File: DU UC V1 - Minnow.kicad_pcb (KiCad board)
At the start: 4 copper layers, 30 x 69.6 mm, 158 parts, among them J1701 MicroUSB, J1801 Conn_01x06_Pin, J1802 Conn_01x04_Pin, J201 SODIMM-260, Q1301 BSS84, Q1501 BSS84, Q1502 BSS84, Q1701 MMBT3904, Q701 BSS84, Q702 BSS84, SW401 STLINK_RST, SW501 MCU_RST, U1101 74HC4051, U1401 TPS25961, U1402 TPS25961, U1501 TCAN334G, U1701 PSM712-LF-T7, U301 TPS7B8733QKVURQ1, U401 STM32F103CBTx, U501 STM32L552ZET6Q, U701 TCAN334G, U901 MX25R3235FM2xx1, Y401 8MHz 5pF, Y501 32.768kHz, 1.2pF, Y502 16MHz, 7pF

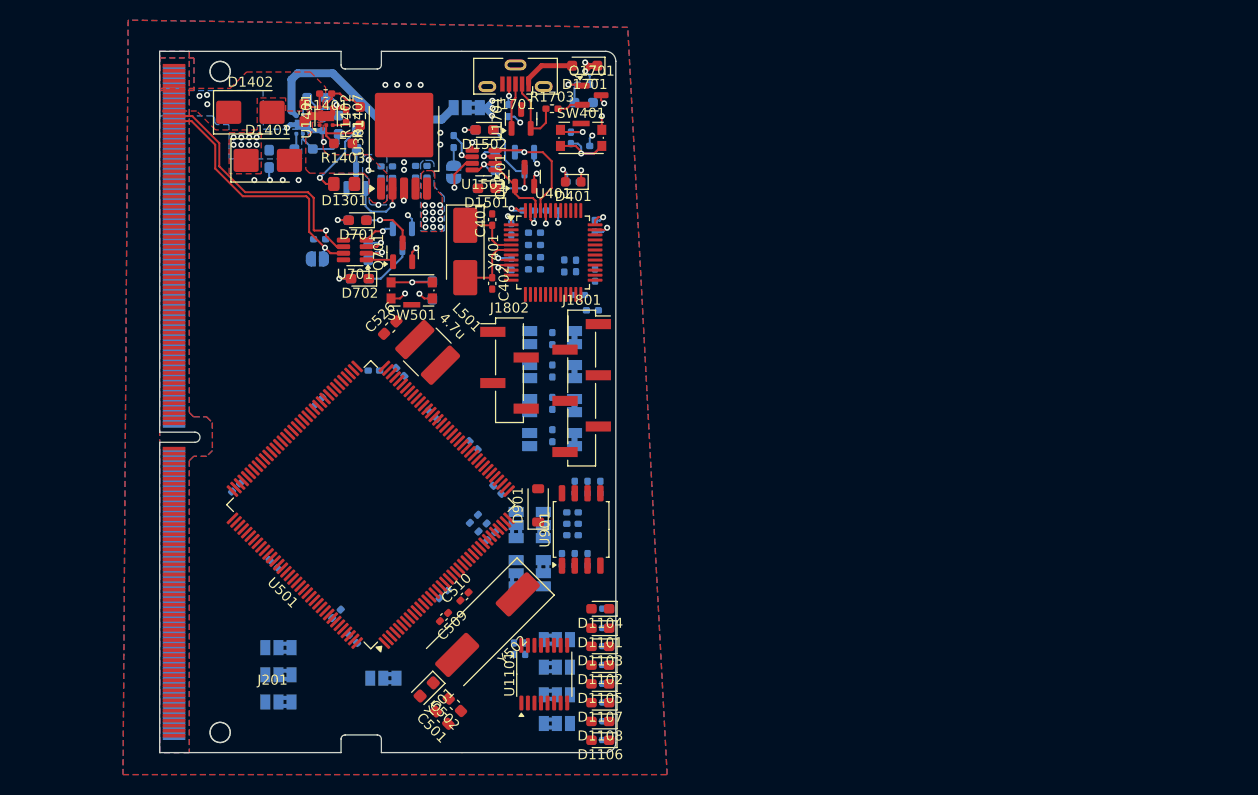
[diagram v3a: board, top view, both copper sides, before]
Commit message: i fucken rerouted everything and redid the pinout like 3x, half routed GPIOs
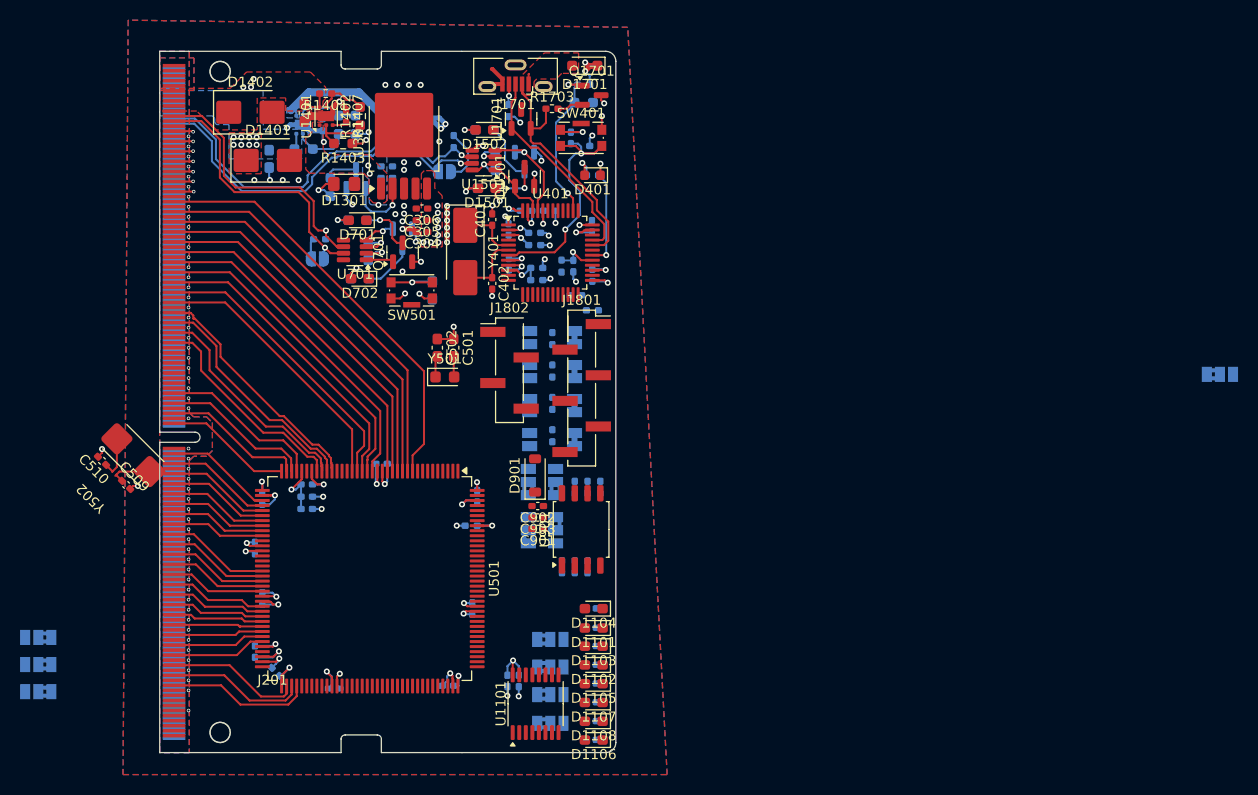
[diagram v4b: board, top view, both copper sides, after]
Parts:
- removed C526: 4.7u, Capacitor_SMD:C_0603_1608Metric_Pad1.08x0.95mm_HandSolder
- removed L501: 4.7u, bfr_inductors:BWVS005050404R7M00
- C304, C305, C306, C901, C902, C903: moved to F.Cu
- Y502: footprint Crystal:Crystal_SMD_HC49-SD -> bfr_crystals:ABM3-16.000MHZ-D2Y-T
- moved JP504 88.3 mm to (182.7, 99.1), turned to 0 degrees
- moved Y502 39.0 mm to (74.8, 107.1), turned to 135 degrees
- moved C510 38.4 mm to (71.7, 107.6), turned to 135 degrees
- moved C501 36.7 mm to (106.6, 96.4), turned to -90 degrees
- moved C502 35.5 mm to (105.0, 96.4), turned to -90 degrees
- moved C509 34.2 mm to (74.1, 110.0), turned to -45 degrees
- moved C516 31.4 mm to (89.0, 128.6), turned to 135 degrees
- moved C512 31.3 mm to (86.9, 126.6), turned to -90 degrees
- moved Y501 31.1 mm to (105.7, 99.3), turned to 0 degrees
- moved C514 28.8 mm to (106.1, 130.0), turned to 180 degrees
- moved C523 28.5 mm to (94.8, 130.2), turned to 180 degrees
- moved C521 24.9 mm to (87.6, 121.3), turned to 90 degrees
- moved C508 24.0 mm to (86.9, 116.3), turned to 90 degrees
- moved JP501 23.9 mm to (65.4, 127.9)
- moved JP502 23.9 mm to (65.4, 130.5)
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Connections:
- net /CANH_STLINK renamed /STLINK_CAN+
- net /CANL_STLINK renamed /STLINK_CAN-
- J201 pad 102: /SODIMM Connector/PB2 -> /SODIMM Connector/PD1
- J201 pad 103: /SODIMM Connector/PC9 -> /SODIMM Connector/PC1
- J201 pad 106: /SODIMM Connector/PB1 -> /SODIMM Connector/PD0
- J201 pad 107: /SODIMM Connector/PC10 -> /SODIMM Connector/PC2
- J201 pad 110: /SODIMM Connector/PB0 -> /SODIMM Connector/PC13
- J201 pad 111: /SODIMM Connector/PC11 -> /SODIMM Connector/PC3
- J201 pad 114: /SODIMM Connector/PA7 -> /SODIMM Connector/PC12
- J201 pad 115: /SODIMM Connector/PC12 -> /SODIMM Connector/PF12
- J201 pad 118: /SODIMM Connector/PA6 -> /SODIMM Connector/PC11
- J201 pad 119: /SODIMM Connector/PA8 -> /SODIMM Connector/PF13
- J201 pad 122: /SODIMM Connector/PA5 -> /SODIMM Connector/PC10
- J201 pad 123: /SODIMM Connector/PA9 -> /SODIMM Connector/PF14
- J201 pad 126: /SODIMM Connector/PA4 -> /SODIMM Connector/PA15
- J201 pad 127: /SODIMM Connector/PA10 -> /SODIMM Connector/PF15
- J201 pad 130: /SODIMM Connector/PA3 -> /SODIMM Connector/PA10
- J201 pad 131: /SODIMM Connector/PA15 -> /SODIMM Connector/PA0
- J201 pad 134: /SODIMM Connector/PA2 -> /SODIMM Connector/PA9
- J201 pad 135: /SODIMM Connector/PD0 -> /SODIMM Connector/PA1
- J201 pad 138: /SODIMM Connector/PA1 -> /SODIMM Connector/PA8
- J201 pad 139: /SODIMM Connector/PD1 -> /SODIMM Connector/PA2
- J201 pad 142: /SODIMM Connector/PA0 -> /SODIMM Connector/PC9
- J201 pad 143: /SODIMM Connector/PD2 -> /SODIMM Connector/PA3
- J201 pad 146: /SODIMM Connector/PC3 -> /SODIMM Connector/PC8
- J201 pad 147: /SODIMM Connector/PD3 -> /SODIMM Connector/PA4
- J201 pad 150: /SODIMM Connector/PC2 -> /SODIMM Connector/PC7
- J201 pad 151: /SODIMM Connector/PD4 -> /SODIMM Connector/PA5
- J201 pad 154: /SODIMM Connector/PC1 -> /SODIMM Connector/PC6
- J201 pad 155: /SODIMM Connector/PD5 -> /SODIMM Connector/PA6
- J201 pad 158: /SODIMM Connector/PC0 -> /SODIMM Connector/PG6
- J201 pad 159: /SODIMM Connector/PD6 -> /SODIMM Connector/PA7
- J201 pad 162: /SODIMM Connector/PF10 -> /SODIMM Connector/PG5
- J201 pad 163: /SODIMM Connector/PD7 -> /SODIMM Connector/PB0
- J201 pad 166: /SODIMM Connector/PF9 -> /SODIMM Connector/PG4
- J201 pad 167: /SODIMM Connector/PG9 -> /SODIMM Connector/PB1
- J201 pad 170: /SODIMM Connector/PF8 -> /SODIMM Connector/PG3
- J201 pad 171: /SODIMM Connector/PG10 -> /SODIMM Connector/PB2
- J201 pad 174: /SODIMM Connector/PF7 -> /SODIMM Connector/PG2
- J201 pad 175: /SODIMM Connector/PG12 -> /SODIMM Connector/PF11
- J201 pad 178: /SODIMM Connector/PF6 -> /SODIMM Connector/PD15
- J201 pad 179: /SODIMM Connector/PG13 -> /SODIMM Connector/PG0
- J201 pad 182: /SODIMM Connector/PF5 -> /SODIMM Connector/PD14
- J201 pad 183: /SODIMM Connector/PG14 -> /SODIMM Connector/PG1
- J201 pad 186: /SODIMM Connector/PF4 -> /SODIMM Connector/PD13
- J201 pad 187: /SODIMM Connector/PG15 -> /SODIMM Connector/PE7
- J201 pad 190: /SODIMM Connector/PF3 -> /SODIMM Connector/PD12
- J201 pad 191: /SODIMM Connector/PB4 -> /SODIMM Connector/PE8
- J201 pad 194: /SODIMM Connector/PF2 -> /SODIMM Connector/PD11
- J201 pad 195: /SODIMM Connector/PB5 -> /SODIMM Connector/PE9
- J201 pad 198: /SODIMM Connector/PF1 -> /SODIMM Connector/PD10
- J201 pad 199: /SODIMM Connector/PB6 -> /SODIMM Connector/PE10
- J201 pad 202: /SODIMM Connector/PF0 -> /SODIMM Connector/PD9
- J201 pad 203: /SODIMM Connector/PB7 -> /SODIMM Connector/PE11
- J201 pad 206: /SODIMM Connector/PC13 -> /SODIMM Connector/PD8
- J201 pad 207: /SODIMM Connector/PB8 -> /SODIMM Connector/PE12
- J201 pad 211: /SODIMM Connector/PB9 -> /SODIMM Connector/PE13
- J201 pad 215: /SODIMM Connector/PE0 -> /SODIMM Connector/PE14
- J201 pad 219: /SODIMM Connector/PE1 -> /SODIMM Connector/PE15
- J201 pad 223: /SODIMM Connector/PE2 -> /SODIMM Connector/PB10
- J201 pad 227: /SODIMM Connector/PE3 -> /SODIMM Connector/PB11
- J201 pad 231: /SODIMM Connector/PE4 -> /SODIMM Connector/PB13
- J201 pad 235: /SODIMM Connector/PE5 -> /SODIMM Connector/PB14
- J201 pad 239: /SODIMM Connector/PE6 -> /SODIMM Connector/PB15
- J201 pad 27: /SODIMM Connector/PB13 -> /SODIMM Connector/PE0
- J201 pad 30: /SODIMM Connector/PB11 -> /SODIMM Connector/PB9
- J201 pad 31: /SODIMM Connector/PB14 -> /SODIMM Connector/PE1
- J201 pad 34: /SODIMM Connector/PB10 -> /SODIMM Connector/PB8
- J201 pad 35: /SODIMM Connector/PB15 -> /SODIMM Connector/PE2
- J201 pad 38: /SODIMM Connector/PE15 -> /SODIMM Connector/PB7
- J201 pad 39: /SODIMM Connector/PD8 -> /SODIMM Connector/PE3
- J201 pad 42: /SODIMM Connector/PE14 -> /SODIMM Connector/PB6
- J201 pad 43: /SODIMM Connector/PD9 -> /SODIMM Connector/PE4
- J201 pad 46: /SODIMM Connector/PE13 -> /SODIMM Connector/PB5
- J201 pad 47: /SODIMM Connector/PD10 -> /SODIMM Connector/PE5
- J201 pad 50: /SODIMM Connector/PE12 -> /SODIMM Connector/PB4
- J201 pad 51: /SODIMM Connector/PD11 -> /SODIMM Connector/PE6
- J201 pad 54: /SODIMM Connector/PE11 -> /SODIMM Connector/PG15
- J201 pad 55: /SODIMM Connector/PD12 -> /SODIMM Connector/PF0
- J201 pad 58: /SODIMM Connector/PE10 -> /SODIMM Connector/PG14
- J201 pad 59: /SODIMM Connector/PD13 -> /SODIMM Connector/PF1
- J201 pad 62: /SODIMM Connector/PE9 -> /SODIMM Connector/PG13
- J201 pad 63: /SODIMM Connector/PD14 -> /SODIMM Connector/PF2
- J201 pad 66: /SODIMM Connector/PE8 -> /SODIMM Connector/PG12
- J201 pad 67: /SODIMM Connector/PD15 -> /SODIMM Connector/PF3
- J201 pad 70: /SODIMM Connector/PE7 -> /SODIMM Connector/PG10
- J201 pad 71: /SODIMM Connector/PG2 -> /SODIMM Connector/PF4
- J201 pad 74: /SODIMM Connector/PG1 -> /SODIMM Connector/PG9
- J201 pad 75: /SODIMM Connector/PG3 -> /SODIMM Connector/PF5
- J201 pad 78: /SODIMM Connector/PG0 -> /SODIMM Connector/PD7
- J201 pad 79: /SODIMM Connector/PG4 -> /SODIMM Connector/PF6
- J201 pad 82: /SODIMM Connector/PF15 -> /SODIMM Connector/PD6
- J201 pad 83: /SODIMM Connector/PG5 -> /SODIMM Connector/PF7
- J201 pad 86: /SODIMM Connector/PF14 -> /SODIMM Connector/PD5
- J201 pad 87: /SODIMM Connector/PG6 -> /SODIMM Connector/PF8
- J201 pad 90: /SODIMM Connector/PF13 -> /SODIMM Connector/PD4
- J201 pad 91: /SODIMM Connector/PC6 -> /SODIMM Connector/PF9
- J201 pad 94: /SODIMM Connector/PF12 -> /SODIMM Connector/PD3
- J201 pad 95: /SODIMM Connector/PC7 -> /SODIMM Connector/PF10
- J201 pad 98: /SODIMM Connector/PF11 -> /SODIMM Connector/PD2
- J201 pad 99: /SODIMM Connector/PC8 -> /SODIMM Connector/PC0
- U501 pad 143: Net-(C526-Pad1) -> unconnected-(U501H-V15SMPS-Pad143)
- U501 pad 68: +3.3V -> unconnected-(U501H-VDDSMPS-Pad68)
- U501 pad 69: Net-(U501H-VLXSMPS) -> unconnected-(U501H-VLXSMPS-Pad69)
- U501 pad 70: GND -> unconnected-(U501H-VSSSMPS-Pad70)
- U501 pad 72: Net-(C526-Pad1) -> unconnected-(U501H-V15SMPS-Pad72)
- Y502 pad 1: Net-(U501I-PH1/HSE_OSC_OUT) -> Net-(U501I-PH0/HSE_OSC_IN)
- Y502 pad 2: Net-(U501I-PH0/HSE_OSC_IN) -> Net-(U501I-PH1/HSE_OSC_OUT)
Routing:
- net GND: track 41.7 -> 103.1 mm, vias 29 -> 122
- net /SODIMM Connector/PF0: track 0.00 -> 42.2 mm
- net +3.3V: track 27.5 -> 67.2 mm, vias 27 -> 36
- net /SODIMM Connector/PF1: track 0.00 -> 39.7 mm
- net /SODIMM Connector/PF2: track 0.00 -> 38.3 mm
- net /SODIMM Connector/PF3: track 0.00 -> 36.8 mm
- net /SODIMM Connector/PF4: track 0.00 -> 35.4 mm
- net /STLINK_CAN-: track 3.39 -> 37.6 mm
- net /SODIMM Connector/PF5: track 0.00 -> 34.0 mm
- net /STLINK_CAN+: track 4.42 -> 37.8 mm
- net /SODIMM Connector/PF6: track 0.00 -> 32.9 mm
- net /SODIMM Connector/PF7: track 0.00 -> 31.6 mm
- net /SODIMM Connector/PF8: track 0.00 -> 30.2 mm
- net /SODIMM Connector/PF9: track 0.00 -> 28.8 mm
- net /SODIMM Connector/PF10: track 0.00 -> 27.0 mm
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- added copper zone on B.Cu, net /Power/Power Protection/3V3A_PROT
- added copper zone on F.Cu, net /ST-link V2/USB Micro-B/PP5000_VUSB_RAW
- removed copper zone on B.Cu, net +3.3V

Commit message: holy fucking stupid ass why did u put this upon urself
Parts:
- moved JP502 109.0 mm to (163.3, 82.5), turned to -45 degrees
- moved JP501 105.4 mm to (161.4, 84.4), turned to -45 degrees
- moved JP503 101.8 mm to (159.5, 86.3), turned to -45 degrees
- moved R702 54.8 mm to (119.7, 133.6), turned to 90 degrees
- moved D701 54.8 mm to (119.7, 133.6), turned to -90 degrees
- moved R701 51.7 mm to (111.7, 134.0), turned to -90 degrees
- moved JP701 50.9 mm to (113.6, 134.2), turned to -90 degrees
- moved U701 48.5 mm to (112.7, 132.6), turned to -90 degrees
- moved Q701 48.5 mm to (116.5, 133.1)
- moved Q702 48.5 mm to (116.5, 131.7)
- moved C701 46.9 mm to (112.6, 131.4), turned to 0 degrees
- moved D702 46.1 mm to (119.7, 129.8), turned to -90 degrees
- moved R703 46.1 mm to (119.7, 129.8), turned to 90 degrees
- moved C517 36.9 mm to (136.9, 108.3), turned to 180 degrees
- moved SW501 36.6 mm to (136.7, 103.8), turned to 90 degrees
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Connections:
- J201 pad 21: /SODIMM Connector/MCU_CAN- -> GND
- J201 pad 23: /SODIMM Connector/MCU_CAN+ -> GND
- J201 pad 255: unconnected-(J201-Pad255) -> /SODIMM Connector/MCU_CAN-
- J201 pad 257: unconnected-(J201-Pad257) -> /SODIMM Connector/MCU_CAN+
- J201 pad 259: unconnected-(J201-Pad259) -> GND
- U501 pad 103: /STM32L552ZET6Q/Peripherals/CAN2_RX -> /STM32L552ZET6Q/CAN2_RX
- U501 pad 104: /STM32L552ZET6Q/Peripherals/CAN2_TX -> /STM32L552ZET6Q/CAN2_TX
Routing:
- net /SODIMM Connector/PG3: track 0.00 -> 30.6 mm, vias 0 -> 1
- net /SODIMM Connector/PG2: track 0.00 -> 28.2 mm, vias 0 -> 1
- net /SODIMM Connector/PD15: track 0.00 -> 26.3 mm, vias 0 -> 1
- net /ST-link V2/MCO: track 2.05 -> 27.5 mm, vias 0 -> 1
- net /SODIMM Connector/PD14: track 0.00 -> 25.1 mm, vias 0 -> 1
- net /SODIMM Connector/PD8: track 0.00 -> 23.8 mm, vias 0 -> 1
- net /SODIMM Connector/PD9: track 0.00 -> 23.6 mm, vias 0 -> 1
- net /SODIMM Connector/PD10: track 0.00 -> 23.5 mm, vias 0 -> 1
- net /SODIMM Connector/PD11: track 0.00 -> 23.3 mm, vias 0 -> 1
- net /SODIMM Connector/PD13: track 0.00 -> 22.9 mm, vias 0 -> 1
- net /SODIMM Connector/PD12: track 0.00 -> 21.7 mm, vias 0 -> 1
- net /SODIMM Connector/MCU_CAN+: track 27.3 -> 41.7 mm
- net /SODIMM Connector/MCU_CAN-: track 27.1 -> 40.7 mm
- net /STM32L552ZET6Q/CAN2_TX: track 2.73 -> 14.5 mm
- net /STM32L552ZET6Q/CAN2_RX: track 3.09 -> 14.0 mm
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
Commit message: fucking shit bro i like expanded the board by 1mm and it still has no room fuck this bitchass crystal
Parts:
- removed C512: 100n, Capacitor_SMD:C_0402_1005Metric_Pad0.74x0.62mm_HandSolder
- removed J1802: Conn_01x04_Pin, Connector_PinHeader_2.54mm:PinHeader_1x04_P2.54mm_Vertical_SMD_Pin1Left
- C301, C302, C303: moved to F.Cu
- D1701: moved to B.Cu
- J1801: value Conn_01x06_Pin -> Conn_02x05_Odd_Even; footprint Connector_PinHeader_2.54mm:PinHeader_1x06_P2.54mm_Vertical_SMD_Pin1Right -> Connector_PinHeader_2.54mm:PinHeader_2x05_P2.54mm_Vertical_SMD
- moved JP504 66.2 mm to (116.9, 91.9), turned to 180 degrees
- moved JP502 38.1 mm to (138.6, 111.5), turned to 180 degrees
- moved JP501 33.4 mm to (138.6, 108.8), turned to 180 degrees
- moved JP503 28.8 mm to (138.6, 106.1), turned to 180 degrees
- moved SW501 22.9 mm to (120.5, 119.9), turned to 0 degrees
- moved JP1201 22.1 mm to (131.3, 105.2)
- moved JP1202 22.1 mm to (139.7, 105.2)
- moved JP1203 22.1 mm to (136.9, 105.2)
- moved JP1204 22.1 mm to (134.2, 105.2)
- moved R1301 20.9 mm to (113.4, 71.9), turned to 180 degrees
- moved D1301 20.6 mm to (113.3, 69.3)
- moved JP1808 20.5 mm to (123.3, 95.8), turned to 180 degrees
- moved JP1805 20.3 mm to (113.1, 95.8), turned to 180 degrees
- moved JP1807 20.1 mm to (119.9, 95.8), turned to 180 degrees
- moved JP1806 20.1 mm to (116.5, 95.8), turned to 180 degrees
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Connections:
- J1801 pad 1: Net-(J1801-Pin_1) -> /5V_RAW
- J1801 pad 2: Net-(J1801-Pin_2) -> GND
- J1801 pad 3: GND -> /ST-link V2/MCU_TCK
- J1801 pad 5: Net-(J1801-Pin_5) -> /ST-link V2/MCU_TMS
- J201 pad 212: /NOR Flash/WRITE_PROT -> GND
- J201 pad 216: /NOR Flash/HOLD -> GND
- R1801 pad 2: Net-(J1801-Pin_1) -> /5V_RAW
- R1802 pad 1: Net-(J1801-Pin_2) -> Net-(J1801-Pin_4)
- R1803 pad 1: Net-(J1801-Pin_4) -> Net-(J1801-Pin_6)
- R1804 pad 1: Net-(J1801-Pin_5) -> Net-(J1801-Pin_8)
- R1805 pad 1: Net-(J1801-Pin_6) -> Net-(J1801-Pin_10)
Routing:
- net /SODIMM Connector/PB8: track 0.00 -> 62.6 mm, vias 0 -> 1
- net /SODIMM Connector/PB9: track 0.00 -> 61.0 mm, vias 0 -> 1
- net /SODIMM Connector/PB7: track 0.00 -> 61.0 mm, vias 0 -> 1
- net /SODIMM Connector/PB5: track 0.00 -> 57.5 mm, vias 0 -> 1
- net /SODIMM Connector/PB6: track 0.00 -> 56.4 mm, vias 0 -> 1
- net /SODIMM Connector/PE0: track 1.92 -> 58.1 mm, vias 1 -> 0
- net /SODIMM Connector/PG15: track 0.00 -> 56.0 mm, vias 0 -> 1
- net /SODIMM Connector/PB4: track 0.00 -> 56.0 mm, vias 0 -> 1
- net /SODIMM Connector/PG14: track 0.00 -> 55.8 mm, vias 0 -> 1
- net /SODIMM Connector/PE1: track 1.91 -> 54.9 mm, vias 1 -> 0
- net /SODIMM Connector/PG13: track 0.00 -> 52.0 mm, vias 0 -> 1
- net /SODIMM Connector/PG12: track 0.00 -> 51.6 mm, vias 0 -> 1
- net /SODIMM Connector/PE2: track 1.90 -> 52.7 mm, vias 1 -> 2
- net /SODIMM Connector/PE3: track 1.90 -> 52.2 mm, vias 1 -> 2
- net /SODIMM Connector/PE4: track 1.90 -> 49.4 mm, vias 1 -> 2
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- removed copper zone on F.Cu, net +3.3V
- removed copper zone on B.Cu, net /Power/Power Protection/5V_PROT
- removed copper zone on F.Cu, net /Power/Power Protection/5V_PROT

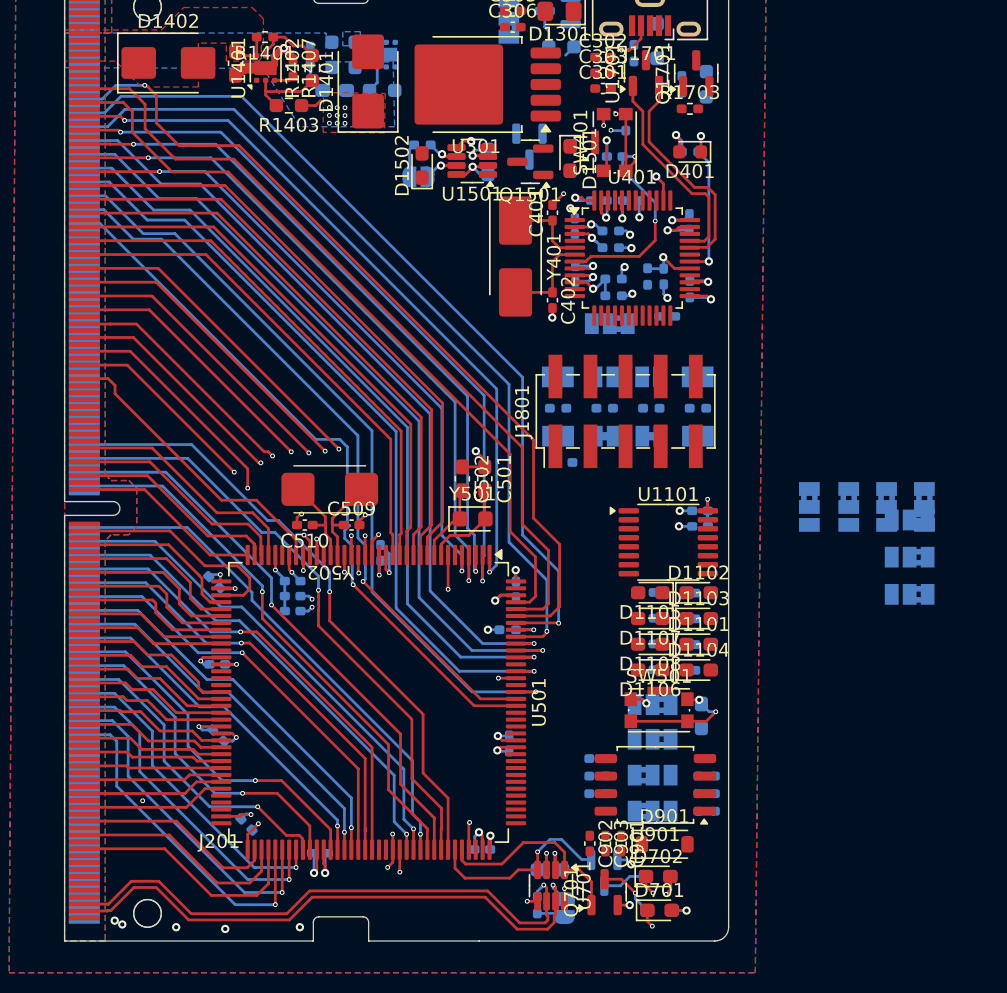
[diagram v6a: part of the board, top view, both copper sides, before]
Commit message: slimed out gpio conns, changed to 6layer
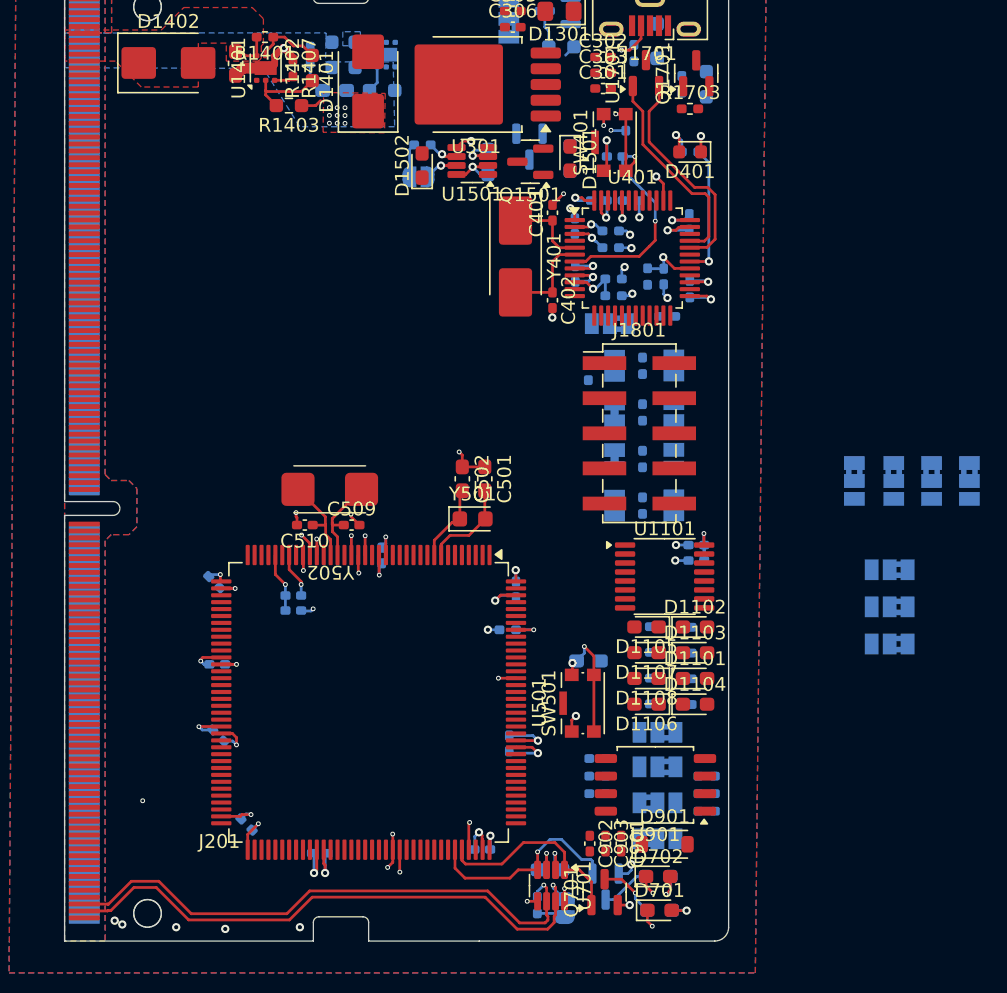
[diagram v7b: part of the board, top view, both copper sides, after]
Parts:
- removed C507: 100n, Capacitor_SMD:C_0402_1005Metric_Pad0.74x0.62mm_HandSolder
- moved JP1808 9.45 mm to (121.5, 105.1), turned to 90 degrees
- moved C517 9.09 mm to (115.4, 116.3), turned to 0 degrees
- moved JP1805 8.44 mm to (121.5, 95.0), turned to 90 degrees
- moved R1805 8.11 mm to (119.3, 105.1), turned to 90 degrees
- moved JP1804 7.85 mm to (117.2, 105.1), turned to -90 degrees
- moved R1802 6.84 mm to (119.3, 95.0), turned to 90 degrees
- moved R1801 6.78 mm to (115.3, 95.4), turned to 90 degrees
- moved JP1801 6.53 mm to (117.2, 95.0), turned to -90 degrees
- moved JP1807 6.15 mm to (121.5, 101.7), turned to 90 degrees
- moved JP1806 5.63 mm to (121.5, 98.3), turned to 90 degrees
- moved SW501 5.54 mm to (115.0, 119.4), turned to 90 degrees
- moved JP501 3.88 mm to (137.2, 112.4)
- moved JP502 3.88 mm to (137.2, 115.1)
- moved JP503 3.88 mm to (137.2, 109.7)
- moved JP1201 3.76 mm to (134.6, 103.3)
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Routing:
- net /SODIMM Connector/PB8: track 62.6 -> 0.00 mm, vias 1 -> 0
- net /SODIMM Connector/PB9: track 61.0 -> 0.00 mm, vias 1 -> 0
- net /SODIMM Connector/PB7: track 61.0 -> 0.00 mm, vias 1 -> 0
- net /SODIMM Connector/PE0: track 58.1 -> 0.00 mm
- net /SODIMM Connector/PB5: track 57.5 -> 0.00 mm, vias 1 -> 0
- net /SODIMM Connector/PB6: track 56.4 -> 0.00 mm, vias 1 -> 0
- net /SODIMM Connector/PG15: track 56.0 -> 0.00 mm, vias 1 -> 0
- net /SODIMM Connector/PB4: track 56.0 -> 0.00 mm, vias 1 -> 0
- net /SODIMM Connector/PG14: track 55.8 -> 0.00 mm, vias 1 -> 0
- net /SODIMM Connector/PE1: track 54.9 -> 0.00 mm
- net /SODIMM Connector/PE2: track 52.7 -> 0.00 mm, vias 2 -> 0
- net /SODIMM Connector/PE3: track 52.2 -> 0.00 mm, vias 2 -> 0
- net /SODIMM Connector/PG13: track 52.0 -> 0.00 mm, vias 1 -> 0
- net /SODIMM Connector/PG12: track 51.6 -> 0.00 mm, vias 1 -> 0
- net /SODIMM Connector/PE4: track 49.4 -> 0.00 mm, vias 2 -> 0
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- added copper zone on In3.Cu, net +3.3V
- added copper zone on In4.Cu, net GND
- removed copper zone on In2.Cu, net +3.3V
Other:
- copper layers 4 -> 6
